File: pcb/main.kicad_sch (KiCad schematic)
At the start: 49 parts, among them Q1 BC337, U1 LM358, U2 LM358, U3 LM358, U4 LM358, U5 LM358, U6 LM358

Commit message: Updated schematics with test points and power filtering.
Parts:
- added C18: 47n, Capacitor_SMD:C_1206_3216Metric_Pad1.33x1.80mm_HandSolder, symbol Device:C_Small
- added C19: 10n, Capacitor_SMD:C_1206_3216Metric_Pad1.33x1.80mm_HandSolder, symbol Device:C_Small
- added C20: 1n, Capacitor_SMD:C_1206_3216Metric_Pad1.33x1.80mm_HandSolder, symbol Device:C_Small
- added C6: 1u, Capacitor_SMD:C_1206_3216Metric_Pad1.33x1.80mm_HandSolder, symbol Device:C_Small
- added C7: 220n, Capacitor_SMD:C_1206_3216Metric_Pad1.33x1.80mm_HandSolder, symbol Device:C_Small
- added C8: 470n, Capacitor_SMD:C_1206_3216Metric_Pad1.33x1.80mm_HandSolder, symbol Device:C_Small
- added C9: 100n, Capacitor_SMD:C_1206_3216Metric_Pad1.33x1.80mm_HandSolder, symbol Device:C_Small
- added FB1: 100R @ 100MHz, symbol Device:FerriteBead_Small
- added J1: Conn_02x02_Row_Letter_First, Connector_PinHeader_2.54mm:PinHeader_2x02_P2.54mm_Vertical, symbol Connector_Generic:Conn_02x02_Row_Letter_First
- added J2: Conn_02x03_Row_Letter_First, Connector_PinHeader_2.54mm:PinHeader_2x03_P2.54mm_Vertical, symbol Connector_Generic:Conn_02x03_Row_Letter_First
- added L1: 20m, symbol Device:L
- added TP10, TP11, TP12, TP13, TP14, TP15, TP16, TP17, TP18, TP2, TP3, TP4, TP5, TP6, TP7, TP8, TP9: TestPoint, TestPoint:TestPoint_Bridge_Pitch2.54mm_Drill0.7mm, symbol Connector:TestPoint
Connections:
- net signal is gone; now on an unnamed net: U6.1
- net +5V: now also J1.a1 (Pin_a1), J1.a2 (Pin_a2); no longer D1.1 (K), R1.1, R2.1, R4.1, U1.8 (V+), U2.8 (V+), U3.8 (V+), U4.8 (V+), U5.8 (V+)
- net GND: now also C18.2, C19.2, C20.2, C6.2, C7.2, C8.2, C9.2
- net at C4.1, C5.1, D5.1 (K)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: now also TP13.1
- net at C2.1, C3.1, D4.1 (K)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: now also TP14.1
- net at C12.2, R11.1, R12.1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: now also TP7.1
- net at C16.2, D5.2 (A), U5.6 (-)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: now also TP12.1
- net at R14.1, R16.1, U4.1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: now also TP8.1
- net at C14.2, D4.2 (A), U5.1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: now also TP11.1
- net at RV4.2, U3.3 (+): now also TP9.1
- net at RV3.2, U1.5 (+), U2.2 (-)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: now also TP5.1
- net at C1.1, Q1.1 (C), R1.2: now also TP2.1
- net at RV2.1, U1.1, U1.2 (-): now also TP3.1
- net at R13.2, RV4.3, U3.5 (+): now also TP10.1
- net at R6.2, RV2.3, U1.7: now also TP4.1
- net at A1.30 (VIN): now also TP18.1
- net at A1.5 (D2): now also TP15.1
- net at A1.6 (D3): now also TP16.1
- net at A1.7 (D4): now also TP17.1
- net at C10.2, R8.1, R9.2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: now also TP6.1
- new net: J1.b1 (Pin_b1), J2.a1 (Pin_a1), J2.a2 (Pin_a2), J2.a3 (Pin_a3)
- new net: J2.b3 (Pin_b3), L1.2
- new net: FB1.1, J2.b1 (Pin_b1)
- new net +5VA: C18.1, C19.1, C20.1, C6.1, C7.1, C8.1, C9.1, D1.1 (K), FB1.2, J1.b2 (Pin_b2), J2.b2 (Pin_b2), L1.1, R1.1, R2.1, R4.1, U1.8 (V+), U2.8 (V+), U3.8 (V+), U4.8 (V+), U5.8 (V+)
- no-connect marks 27 -> 23
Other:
- note added: "MCU."
- note added: "Power."
- moved on the sheet: A1, C1, C10, C11, C12, C13, C14, C15, C16, C17, C2, C3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

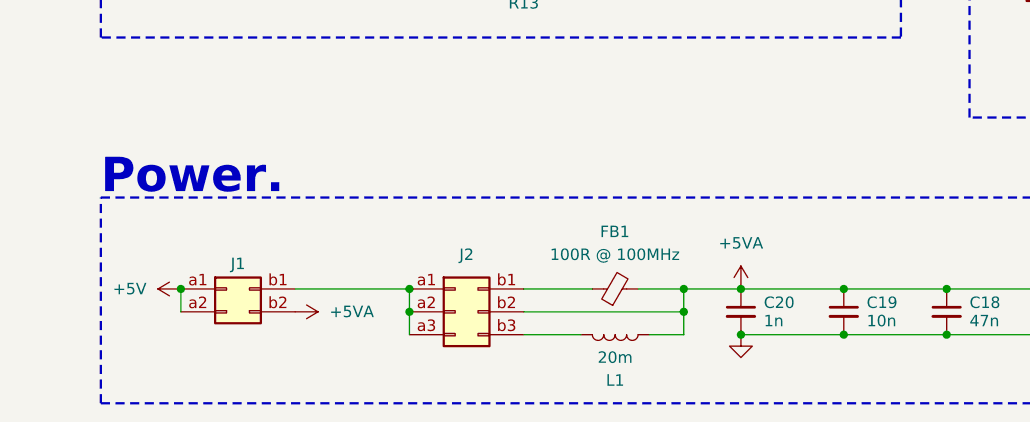
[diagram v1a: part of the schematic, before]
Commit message: Placed the touchpoints and power stuff.
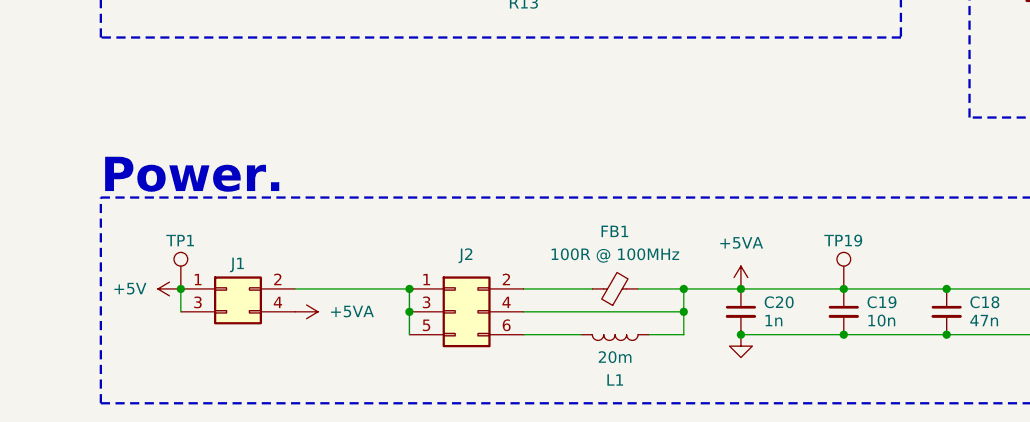
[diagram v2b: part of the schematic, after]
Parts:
- added TP1, TP19: TestPoint, TestPoint:TestPoint_Bridge_Pitch2.54mm_Drill0.7mm, symbol Connector:TestPoint
- FB1: footprint (none) -> Inductor_SMD:L_1206_3216Metric_Pad1.42x1.75mm_HandSolder
- J1: symbol Connector_Generic:Conn_02x02_Row_Letter_First -> Connector_Generic:Conn_02x02_Odd_Even
- J2: symbol Connector_Generic:Conn_02x03_Row_Letter_First -> Connector_Generic:Conn_02x03_Odd_Even
- L1: footprint (none) -> Inductor_THT:L_Radial_D10.0mm_P5.00mm_Neosid_SD12k_style3
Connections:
- net +5V: now also J1.1 (Pin_1), J1.3 (Pin_3), TP1.1; no longer J1.a1 (Pin_a1), J1.a2 (Pin_a2)
- net +5VA: now also J1.4 (Pin_4), J2.4 (Pin_4), TP19.1; no longer J1.b2 (Pin_b2), J2.b2 (Pin_b2)
- net at L1.2: now also J2.6 (Pin_6); no longer J2.b3 (Pin_b3)
- net at FB1.1: now also J2.2 (Pin_2); no longer J2.b1 (Pin_b1)
- new net: J1.2 (Pin_2), J2.1 (Pin_1), J2.3 (Pin_3), J2.5 (Pin_5)
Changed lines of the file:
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@@
 	)
 	(symbol
-		(lib_id "Connector_Generic:Conn_02x02_Row_Letter_First")
+		(lib_id "Connector_Generic:Conn_02x02_Odd_Even")
 		(at 278.13 269.24 0)
 		(unit 1)
@@
 			)
 		)
-		(property "Description" "Generic connector, double row, 02x02, row letter first pin numbering scheme (pin number consists of a letter for the row and a number for the pin index in this row. a1, ..., aN; b1, ..., bN), script generated (kicad-library-utils/schlib/autogen/connector/)"
+		(property "Description" "Generic connector, double row, 02x02, odd/even pin numbering scheme (row 1 odd numbers, row 2 even numbers), script generated (kicad-library-utils/schlib/autogen/connector/)"
 			(at 278.13 269.24 0)
 			(effects
@@
 			)
 		)
-		(pin "b1"
+		(pin "2"
 		)
-		(pin "a2"
+		(pin "3"
 		)
-		(pin "b2"
+		(pin "1"
 		)
-		(pin "a1"
+		(pin "4"
 		)
 		(instances
@@
 	)
 	(symbol
+		(lib_id "Connector:TestPoint")
+		(at 273.05 269.24 0)
+		(mirror y)
+		(unit 1)
+		(exclude_from_sim no)
+		(in_bom yes)
+		(on_board yes)
+		(dnp no)
+		(property "Reference" "TP1"
+			(at 273.05 263.906 0)
+			(effects
+				(font
+					(size 1.27 1.27)
+				)
+			)
+		)
+		(property "Value" "TestPoint"
+			(at 270.51 267.2079 0)
+			(effects
+				(font
+					(size 1.27 1.27)
+				)
+				(justify left)
+				(hide yes)
+			)
+		)
+		(property "Footprint" "TestPoint:TestPoint_Bridge_Pitch2.54mm_Drill0.7mm"
+			(at 267.97 269.24 0)
+			(effects
+				(font
+					(size 1.27 1.27)
+				)
+				(hide yes)
+			)
+		)
+		(property "Datasheet" "~"
+			(at 267.97 269.24 0)
+			(effects
+				(font
+					(size 1.27 1.27)
+				)
+				(hide yes)
+			)
+		)
+		(property "Description" "test point"
+			(at 273.05 269.24 0)
+			(effects
+				(font
+					(size 1.27 1.27)
+				)
+				(hide yes)
+			)
+		)
+		(pin "1"
+		)
+		(instances
+			(project "main"
+				(path "/5b58330d-a0f3-43de-a3af-b429ccd24917"
+					(reference "TP1")
+					(unit 1)
+				)
+			)
+		)
+	)
+	(symbol
 		(lib_id "power:GND")
 		(at 298.45 187.96 0)
@@
 			)
 		)
-		(property "Footprint" ""
+		(property "Footprint" "Inductor_THT:L_Radial_D10.0mm_P5.00mm_Neosid_SD12k_style3"
 			(at 321.31 274.32 0)
 			(effects
@@
 			)
 		)
-		(property "Footprint" ""
+		(property "Footprint" "Inductor_SMD:L_1206_3216Metric_Pad1.42x1.75mm_HandSolder"
 			(at 321.31 271.018 90)
 			(effects
@@
 	(symbol
 		(lib_id "Connector:TestPoint")
+		(at 346.71 269.24 0)
+		(mirror y)
+		(unit 1)
+		(exclude_from_sim no)
+		(in_bom yes)
+		(on_board yes)
+		(dnp no)
+		(property "Reference" "TP19"
+			(at 346.71 263.906 0)
+			(effects
+				(font
+					(size 1.27 1.27)
+				)
+			)
+		)
+		(property "Value" "TestPoint"
+			(at 344.17 267.2079 0)
+			(effects
+				(font
+					(size 1.27 1.27)
+				)
+				(justify left)
+				(hide yes)
+			)
+		)
+		(property "Footprint" "TestPoint:TestPoint_Bridge_Pitch2.54mm_Drill0.7mm"
+			(at 341.63 269.24 0)
+			(effects
+				(font
+					(size 1.27 1.27)
+				)
+				(hide yes)
+			)
+		)
+		(property "Datasheet" "~"
+			(at 341.63 269.24 0)
+			(effects
+				(font
+					(size 1.27 1.27)
+				)
+				(hide yes)
+			)
+		)
+		(property "Description" "test point"
+			(at 346.71 269.24 0)
+			(effects
+				(font
+					(size 1.27 1.27)
+				)
+				(hide yes)
+			)
+		)
+		(pin "1"
+		)
+		(instances
+			(project "main"
+				(path "/5b58330d-a0f3-43de-a3af-b429ccd24917"
+					(reference "TP19")
+					(unit 1)
+				)
+			)
+		)
+	)
+	(symbol
+		(lib_id "Connector:TestPoint")
 		(at 511.81 201.93 0)
 		(mirror y)
@@
 	)
 	(symbol
-		(lib_id "Connector_Generic:Conn_02x03_Row_Letter_First")
+		(lib_id "Connector_Generic:Conn_02x03_Odd_Even")
 		(at 303.53 271.78 0)
 		(unit 1)
@@
 			)
 		)
-		(property "Description" "Generic connector, double row, 02x03, row letter first pin numbering scheme (pin number consists of a letter for the row and a number for the pin index in this row. a1, ..., aN; b1, ..., bN), script generated (kicad-library-utils/schlib/autogen/connector/)"
+		(property "Description" "Generic connector, double row, 02x03, odd/even pin numbering scheme (row 1 odd numbers, row 2 even numbers), script generated (kicad-library-utils/schlib/autogen/connector/)"
 			(at 303.53 271.78 0)
 			(effects
@@
 			)
 		)
-		(pin "b1"
+		(pin "6"
 		)
-		(pin "a2"
+		(pin "4"
 		)
-		(pin "b2"
+		(pin "2"
 		)
-		(pin "a1"
+		(pin "1"
 		)
-		(pin "a3"
+		(pin "5"
 		)
-		(pin "b3"
+		(pin "3"
 		)
 		(instances

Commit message: Adjusted potentiometer values and reannotated.
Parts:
- R15: renamed from R16; value 100k -> 20k
- R16: renamed from R17; value 100k -> 20k
- R17: renamed from R13; value 100k -> 20k
- R4: renamed from R15; value 100k -> 20k
- R5: renamed from R14; value 100k -> 20k
- RV1: renamed from RV3; value 100k -> 1k
- renumbered C17 to C10, C15 to C11, C5 to C12, C4 to C13, C18 to C14, C20 to C15, C7 to C16, C9 to C17, C8 to C18, C10 to C2, C6 to C20, C2 to C4, C12 to C5, C11 to C6, C13 to C7, C16 to C8, C14 to C9, D5 to D4, D4 to D5, R2 to R1, R11 to R10, R7 to R11, R10 to R12, R9 to R13, R12 to R14, R19 to R18, R5 to R19, R8 to R2, R6 to R3, R18 to R6, R3 to R7, R4 to R8, R1 to R9, RV4 to RV3, TP2 to TP1, TP18 to TP10, TP14 to TP11, TP13 to TP12, TP12 to TP13, TP16 to TP14, TP17 to TP15, TP1 to TP16, TP5 to TP17, TP15 to TP18, TP4 to TP2, TP6 to TP3, TP3 to TP4, TP9 to TP5, TP8 to TP6, TP10 to TP8, TP11 to TP9, U5 to U4, U4 to U5

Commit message: Routed things out.
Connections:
- net +5V: no longer RV3.1
- net +5VA: now also RV3.1
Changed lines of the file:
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@@
 	)
 	(symbol
-		(lib_id "power:+5V")
+		(lib_id "power:+5VA")
 		(at 274.32 229.87 90)
 		(unit 1)
@@
 			)
 		)
-		(property "Value" "+5V"
+		(property "Value" "+5VA"
 			(at 270.51 229.8699 90)
 			(effects
@@
 			)
 		)
-		(property "Description" "Power symbol creates a global label with name \"+5V\""
+		(property "Description" "Power symbol creates a global label with name \"+5VA\""
 			(at 274.32 229.87 0)
 			(effects
